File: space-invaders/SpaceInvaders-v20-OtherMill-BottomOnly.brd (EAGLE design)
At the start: 91.4 x 91.4 mm, 26 parts, among them J2-J4 TM4C123GXL, J3-J1 TM4C123GXL, J5 NOKIA_5110, J6 NOKIA_5110, J7 9V, U1 LM7805CT

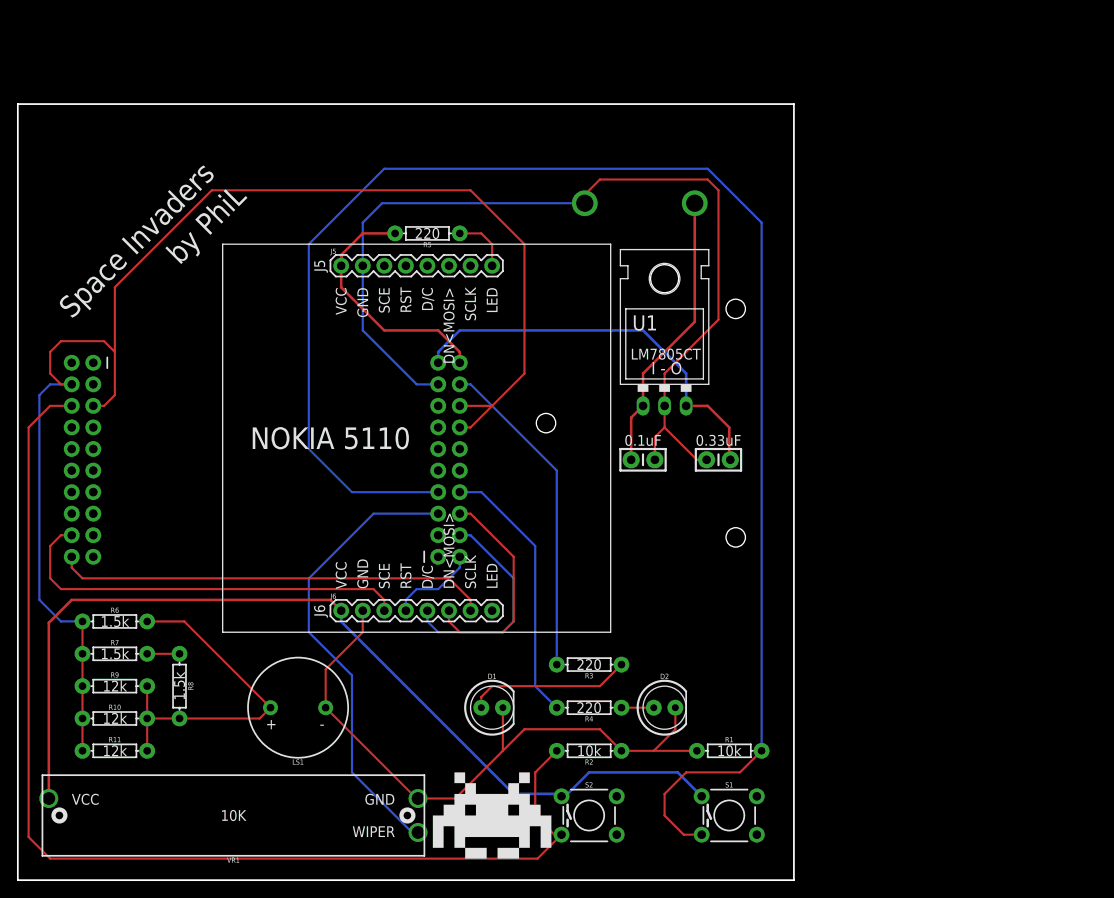
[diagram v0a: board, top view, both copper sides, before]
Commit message: Add versions to file names & Edit stuff
Add versions to file names.
Center Nokia5110 & Edit traces thereof.
Add holes for 9V battery's wires to come through.
v2.1: Replace "SpaceInvaders," "by PhiL," and the sprite icon by Top &
Bottom layers.
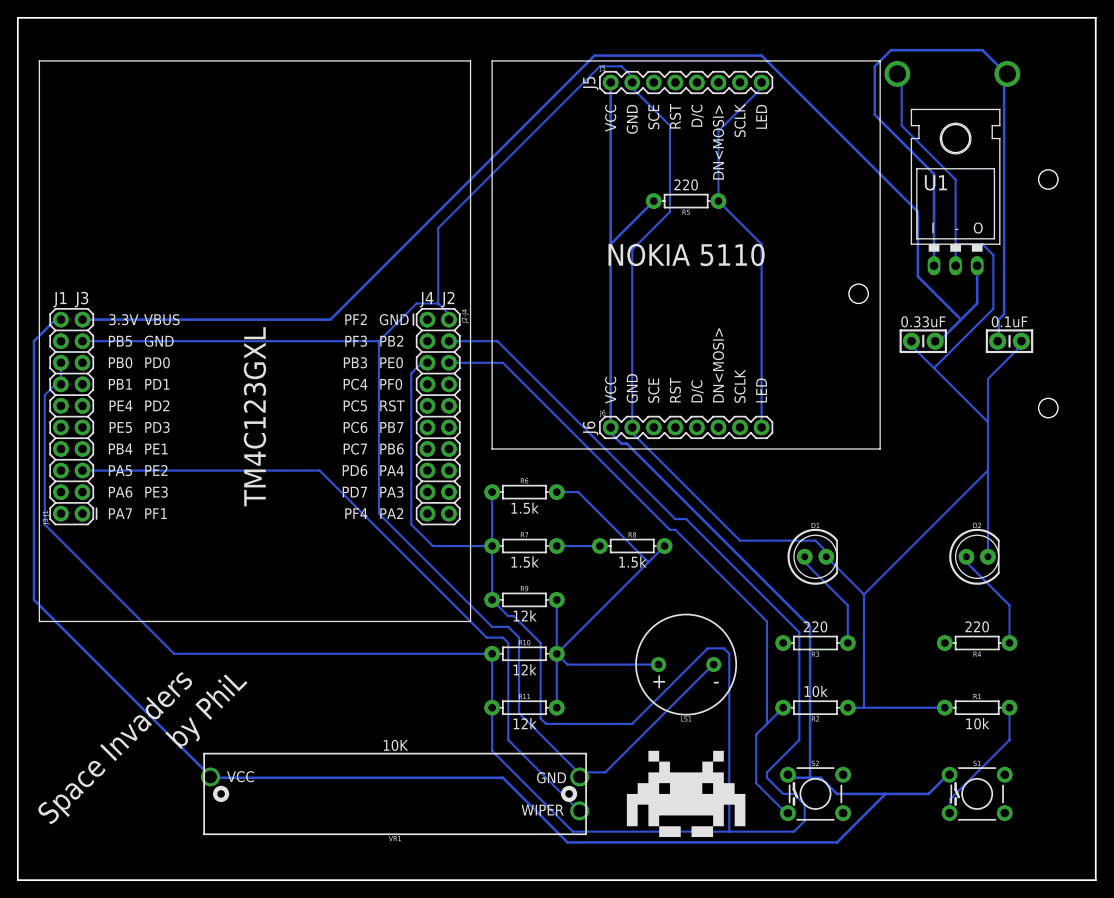
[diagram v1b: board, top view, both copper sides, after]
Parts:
- J5, J6: value NOKIA_5110 -> Nokia_5110
- moved R8 55.8 mm to (72.4, 39.4), turned to 0 degrees
- moved R6 50.6 mm to (59.7, 45.7)
- moved R7 49.9 mm to (59.7, 39.4)
- moved R9 49.3 mm to (59.7, 33.0)
- moved R10 48.9 mm to (59.7, 26.7)
- moved R11 48.5 mm to (59.7, 20.3)
- moved R4 46.4 mm to (113.0, 27.9)
- moved LS1 46.0 mm to (78.7, 25.4)
- moved C2 45.4 mm to (116.8, 63.5)
- moved J3-J1 42.2 mm to (7.62, 43.2), flipped to the top
- moved D1 42.0 mm to (94.0, 38.1)
- moved D2 40.9 mm to (113.0, 38.1)
- moved J7 39.9 mm to (95.2, 41.9)
- moved J2-J4 39.7 mm to (48.3, 66.0), flipped to the top
- moved J5 38.4 mm to (69.8, 94.0)
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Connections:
- net DAC renamed PB2
- new net D/C: J6.5
- new net DN<MOSI>: J6.6
- new net RST: J6.4
- new net SCE: J5.3
- new net SCLK: J5.7
- net PA2: no longer J5.7
- net PA3: no longer J5.3
- net PA5: no longer J6.6
- net PA6: no longer J6.5
- net PA7: no longer J6.4
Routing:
- net GND: track 187.8 -> 384.2 mm
- net PE1: track 184.7 -> 15.3 mm
- net PB2: track 164.8 -> 321.4 mm
- net 3.3V: track 142.3 -> 269.5 mm
- net VBUS: track 47.4 -> 145.0 mm
- net PE0: track 132.1 -> 77.5 mm
- net PA2: track 51.1 -> 0.00 mm
- net PA3: track 48.6 -> 0.00 mm
- net 9V: track 33.3 -> 76.0 mm
- net PB5: track 38.5 -> 0.00 mm
- net LED: track 6.88 -> 44.8 mm
- net PB4: track 31.6 -> 0.00 mm
- net PE2: track 54.1 -> 81.9 mm
- net PA6: track 26.0 -> 0.00 mm
- net PA5: track 26.0 -> 0.00 mm
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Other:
- board size 91.4 x 91.4 mm -> 127 x 101.6 mm
- board text added: "I"
- board text added: "O"
- board text removed: "I - O"
- board text removed: "LM7805CT"
